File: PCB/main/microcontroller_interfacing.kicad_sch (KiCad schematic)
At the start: 0 parts

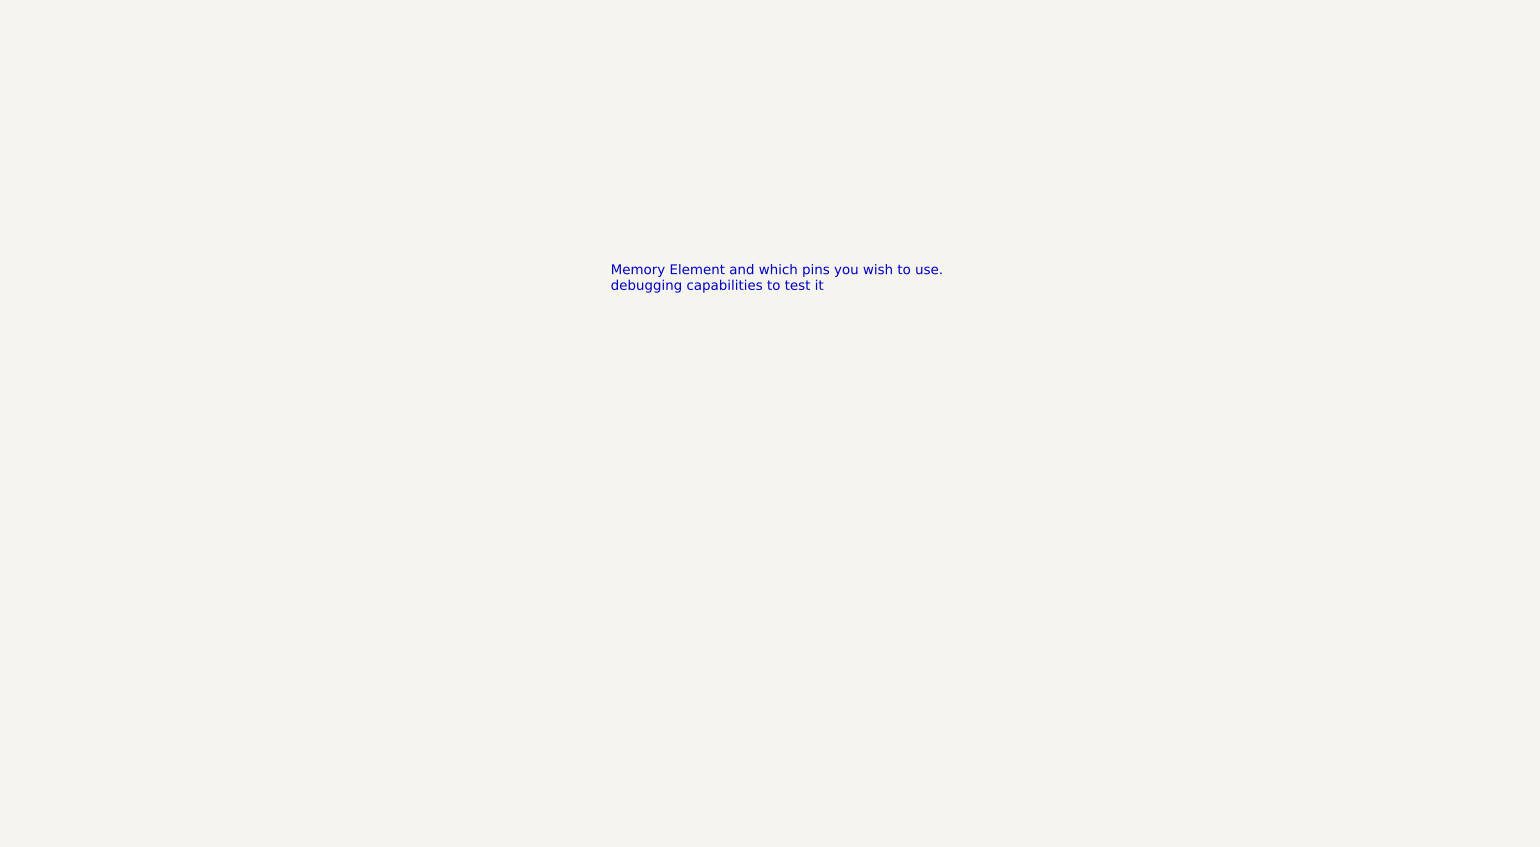
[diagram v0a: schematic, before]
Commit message: Upload draft microcontroller_interfacing.kicad_sch
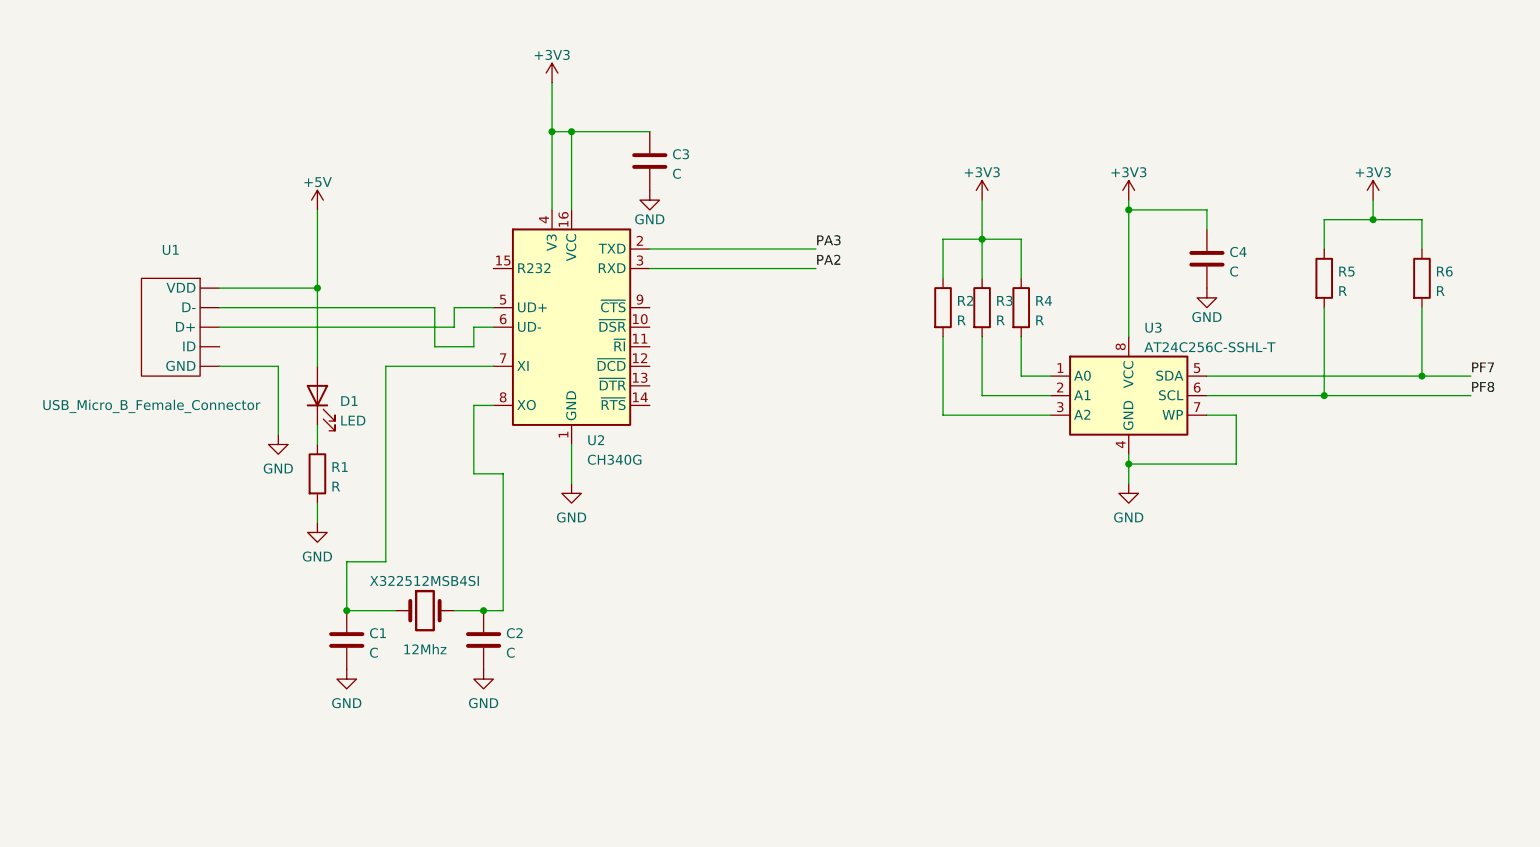
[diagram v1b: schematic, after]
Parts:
- added C1, C2, C3, C4: C, symbol Device:C
- added D1: LED, symbol Device:LED
- added R1, R2, R3, R4, R5, R6: R, symbol Device:R
- added U1: USB_Micro_B_Female_Connector, symbol New_Library:USB_Micro_B_Female_Connector
- added U2: CH340G, Package_SO:SOIC-16_3.9x9.9mm_P1.27mm, symbol Interface_USB:CH340G
- added U3: AT24C256C-SSHL-T, Package_SO:TSSOP-8_4.4x3mm_P0.65mm, symbol Memory_EEPROM:AT24CS01-XHM
- added X322512MSB4SI: 12Mhz, symbol Device:Crystal
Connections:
- new net: C2.1, U2.8 (XO), X322512MSB4SI.2
- new net: R4.2, U3.1 (A0)
- new net: R2.2, U3.3 (A2)
- new net: R3.2, U3.2 (A1)
- new net: C1.1, U2.7 (XI), X322512MSB4SI.1
- new net: D1.1 (K), R1.1
- new net: U1. (VDD), U2.5 (UD+)
- new net: U1. (VDD), U2.6 (UD-)
- new net +3V3: C3.1, C4.1, R2.1, R3.1, R4.1, R5.1, R6.1, U2.16 (VCC), U2.4 (V3), U3.8 (VCC)
- new net +5V: D1.2 (A), U1. (VDD)
- new net GND: C1.2, C2.2, C3.2, C4.2, R1.2, U1. (VDD), U2.1 (GND), U3.4 (GND), U3.7 (WP)
- new net PA2: U2.3 (RXD)
- new net PA3: U2.2 (TXD)
- new net PF7: R6.2, U3.5 (SDA)
- new net PF8: R5.2, U3.6 (SCL)
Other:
- note removed: "Memory Element and which pins you wish to use. debugging capabilities to test it"

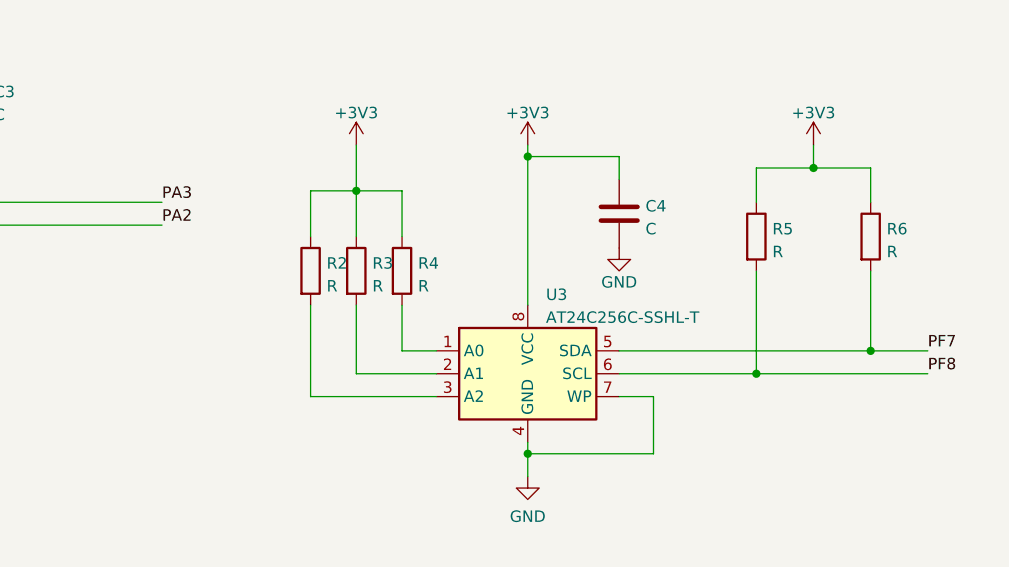
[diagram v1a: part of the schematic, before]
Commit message: Change labels to global labels
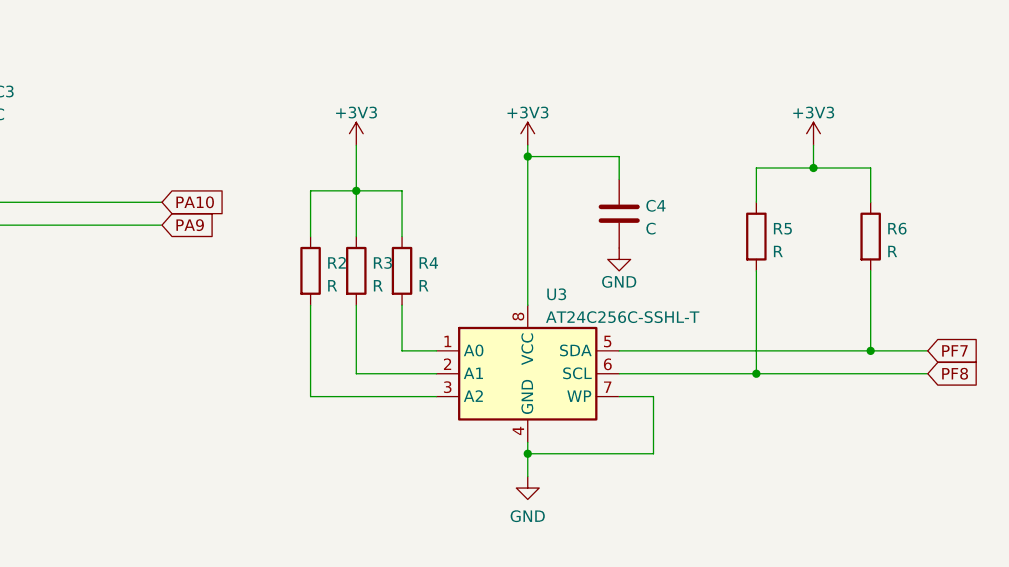
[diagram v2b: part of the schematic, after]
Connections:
- net PA2 renamed PA9
- net PA3 renamed PA10
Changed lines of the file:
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@@
     (stroke (width 0) (type default) (color 0 0 0 0))
   )
-  (label "PA2" (at 156.21 86.36 0)
-    (effects (font (size 1.27 1.27)) (justify left bottom))
+  (global_label "PF8" (shape input) (at 241.3 102.87 0) (fields_autoplaced)
+    (effects (font (size 1.27 1.27)) (justify left))
+    (property "Intersheet References" "${INTERSHEET_REFS}" (id 0) (at 247.2812 102.7906 0)
+      (effects (font (size 1.27 1.27)) (justify left) hide)
+    )
   )
-  (label "PF8" (at 241.3 102.87 0)
-    (effects (font (size 1.27 1.27)) (justify left bottom))
+  (global_label "PA10" (shape input) (at 156.21 83.82 0) (fields_autoplaced)
+    (effects (font (size 1.27 1.27)) (justify left))
+    (property "Intersheet References" "${INTERSHEET_REFS}" (id 0) (at 163.4007 83.7406 0)
+      (effects (font (size 1.27 1.27)) (justify left) hide)
+    )
   )
-  (label "PF7" (at 241.3 100.33 0)
-    (effects (font (size 1.27 1.27)) (justify left bottom))
+  (global_label "PA9" (shape input) (at 156.21 86.36 0) (fields_autoplaced)
+    (effects (font (size 1.27 1.27)) (justify left))
+    (property "Intersheet References" "${INTERSHEET_REFS}" (id 0) (at 162.1912 86.2806 0)
+      (effects (font (size 1.27 1.27)) (justify left) hide)
+    )
   )
-  (label "PA3" (at 156.21 83.82 0)
-    (effects (font (size 1.27 1.27)) (justify left bottom))
+  (global_label "PF7" (shape input) (at 241.3 100.33 0) (fields_autoplaced)
+    (effects (font (size 1.27 1.27)) (justify left))
+    (property "Intersheet References" "${INTERSHEET_REFS}" (id 0) (at 247.2812 100.2506 0)
+      (effects (font (size 1.27 1.27)) (justify left) hide)
+    )
   )
   (symbol (lib_id "power:+3V3") (at 177.8 77.47 0) (unit 1)

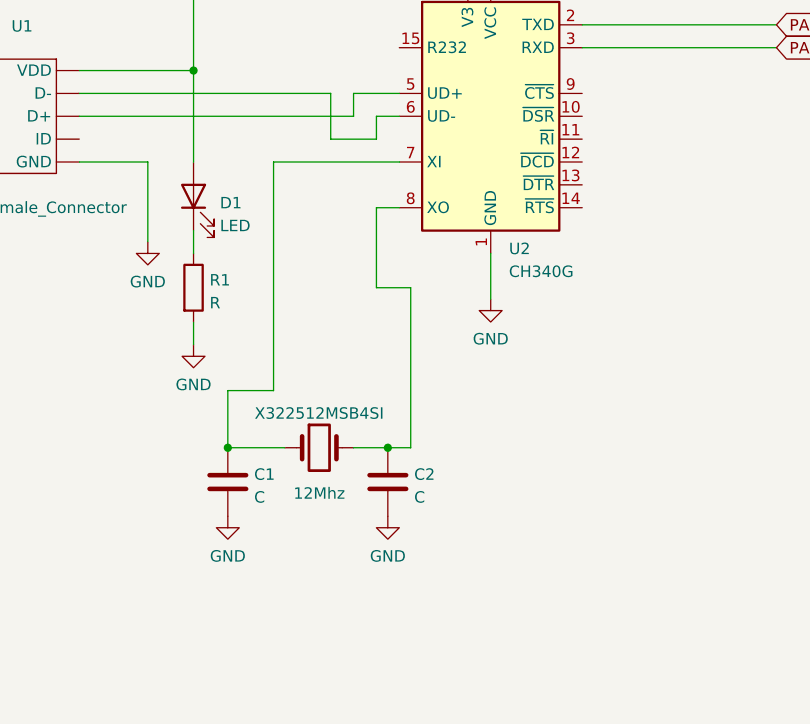
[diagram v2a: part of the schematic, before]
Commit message: Added Kicad Libraries
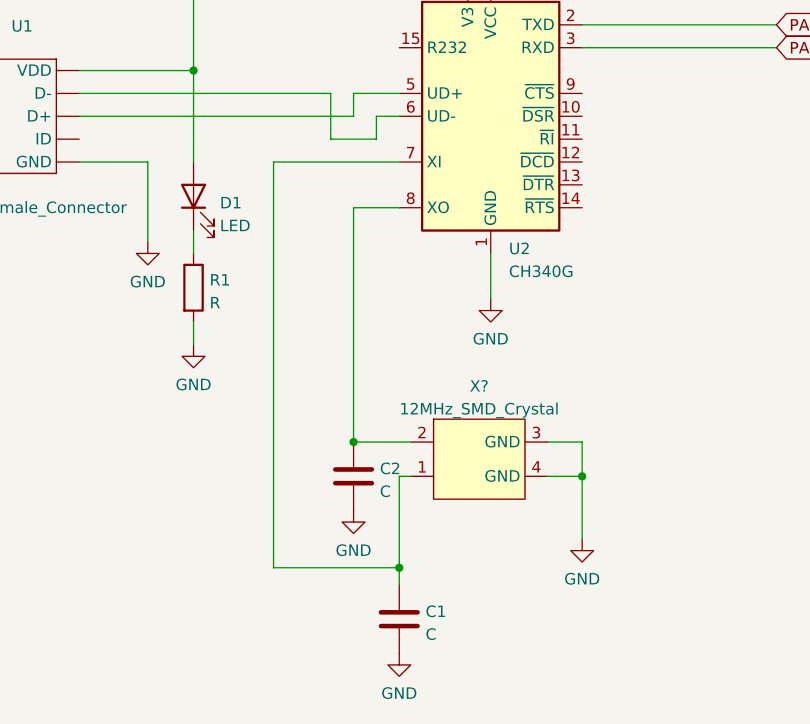
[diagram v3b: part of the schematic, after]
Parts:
- removed X322512MSB4SI: 12Mhz, symbol Device:Crystal
- added X?: 12MHz_SMD_Crystal, symbol Symbol_EEE3088F:12MHz_SMD_Crystal
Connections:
- net GND: now also X?.3 (GND), X?.4 (GND)
- net at C2.1, U2.8 (XO): now also X?.2
- net at C1.1, U2.7 (XI): now also X?.1
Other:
- moved on the sheet: C1, C2

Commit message: Add Kicad footprints and symbols
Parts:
- removed U1: USB_Micro_B_Female_Connector, symbol New_Library:USB_Micro_B_Female_Connector
- added U?: USB_Micro_B_Female_Connector, Footprint_EEE3088F:MICRO-USB-SMD_U254-051T-4BH83-S1S, symbol Symbol_EEE3088F:USB_Micro_B_Female_Connector
- X1: renamed from X?; footprint (none) -> Footprint_EEE3088F:OSC-SMD_4P-L3.2-W2.5-BL
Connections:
- net +5V: now also U?.1 (VDD)
- net GND: now also U?.5 (GND)
- net at U2.5 (UD+): now also U?.3 (D+)
- net at U2.6 (UD-): now also U?.2 (D-)
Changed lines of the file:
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@@
     (pin "1")
+  )
+  (symbol (lib_id "Symbol_EEE3088F:USB_Micro_B_Female_Connector") (at 71.12 93.98 0) (unit 1)
+    (in_bom yes) (on_board yes) (fields_autoplaced)
+    (property "Reference" "U?" (id 0) (at 72.39 83.981 0))
+    (property "Value" "USB_Micro_B_Female_Connector" (id 1) (at 72.39 86.5179 0))
+    (property "Footprint" "Footprint_EEE3088F:MICRO-USB-SMD_U254-051T-4BH83-S1S" (id 2) (at 71.12 93.98 0)
+      (effects (font (size 1.27 1.27)) hide)
+    )
+    (property "Datasheet" "" (id 3) (at 71.12 93.98 0)
+      (effects (font (size 1.27 1.27)) hide)
+    )
+    (pin "1")
+    (pin "2")
+    (pin "3")
+    (pin "4")
+    (pin "5")
+    (pin "6")
   )
   (symbol (lib_id "power:+5V") (at 91.44 78.74 0) (unit 1)
@@
   (symbol (lib_id "Symbol_EEE3088F:12MHz_SMD_Crystal") (at 123.19 131.445 0) (unit 1)
     (in_bom yes) (on_board yes) (fields_autoplaced)
-    (property "Reference" "X?" (id 0) (at 123.19 123.986 0))
+    (property "Reference" "X1" (id 0) (at 123.19 123.986 0))
     (property "Value" "12MHz_SMD_Crystal" (id 1) (at 123.19 126.5229 0))
-    (property "Footprint" "" (id 2) (at 123.19 131.445 0)
+    (property "Footprint" "Footprint_EEE3088F:OSC-SMD_4P-L3.2-W2.5-BL" (id 2) (at 123.19 131.445 0)
       (effects (font (size 1.27 1.27)) hide)
     )
@@
   (symbol (lib_id "power:GND") (at 134.62 140.97 0) (unit 1)
     (in_bom yes) (on_board yes) (fields_autoplaced)
-    (property "Reference" "#PWR?" (id 0) (at 134.62 147.32 0)
+    (property "Reference" "#PWR0114" (id 0) (at 134.62 147.32 0)
       (effects (font (size 1.27 1.27)) hide)
     )
@@
     (pin "1")
   )
-  (symbol (lib_id "New_Library:USB_Micro_B_Female_Connector") (at 71.12 93.98 0) (unit 1)
-    (in_bom yes) (on_board yes)
-    (property "Reference" "U1" (id 0) (at 72.39 83.981 0))
-    (property "Value" "USB_Micro_B_Female_Connector" (id 1) (at 69.85 104.14 0))
-    (property "Footprint" "" (id 2) (at 71.12 93.98 0)
-      (effects (font (size 1.27 1.27)) hide)
-    )
-    (property "Datasheet" "" (id 3) (at 71.12 93.98 0)
-      (effects (font (size 1.27 1.27)) hide)
-    )
-    (pin "")
-    (pin "")
-    (pin "")
-    (pin "")
-    (pin "")
-  )
   (symbol (lib_id "Device:C") (at 114.3 149.86 0) (unit 1)

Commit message: update schematics
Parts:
- removed C3: C, symbol Device:C
- removed R2, R3, R4: R, symbol Device:R
- removed U3: AT24C256C-SSHL-T, Package_SO:TSSOP-8_4.4x3mm_P0.65mm, symbol Memory_EEPROM:AT24CS01-XHM
- added U?: AT24C256C-SSHL-T, Footprint_EEE3088F:SOIC-8_L4.9-W3.9-P1.27-LS6.0-BL, symbol Symbol_EEE3088F:AT24C256C-SSHL-T
- C1, C2: value C -> 33p
- C4: value C -> 0.1u
- D1: footprint (none) -> Footprint_EEE3088F:LED0603-R-RD
- R5, R6: value R -> 10k
- gave numbers to parts that had none: 1
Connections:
- net +3V3: now also U?.8 (VCC)
- net GND: now also U?.1 (A0), U?.2 (A1), U?.3 (A2), U?.4 (GND), U?.7 (WP)
- net PF7: now also U?.5 (SDA)
- net PF8: now also U?.6 (SCL)
